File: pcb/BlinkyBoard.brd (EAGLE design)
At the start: 25.2 x 10 mm, 27 parts, among them Q1 16 MHz

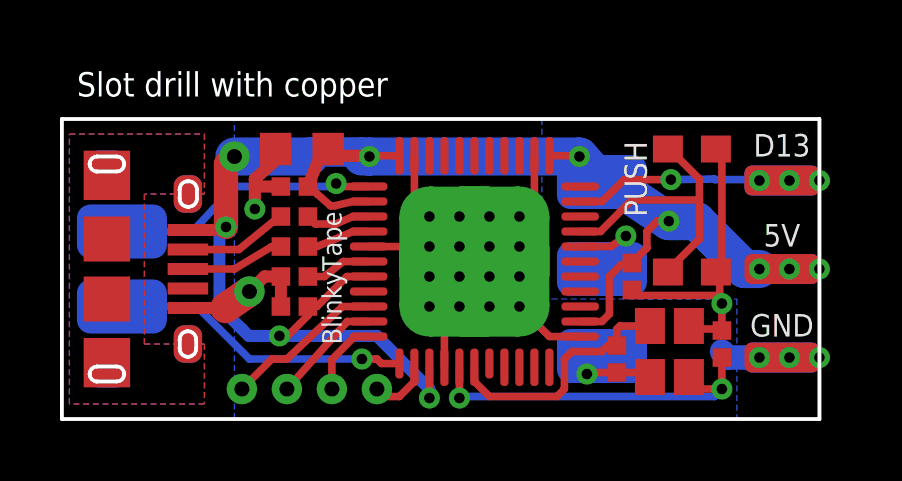
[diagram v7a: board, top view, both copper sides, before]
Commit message: PCB: Make LED connector holes bigger as per Bunnie's suggestion. Move the BlinkyTape logo a bit.
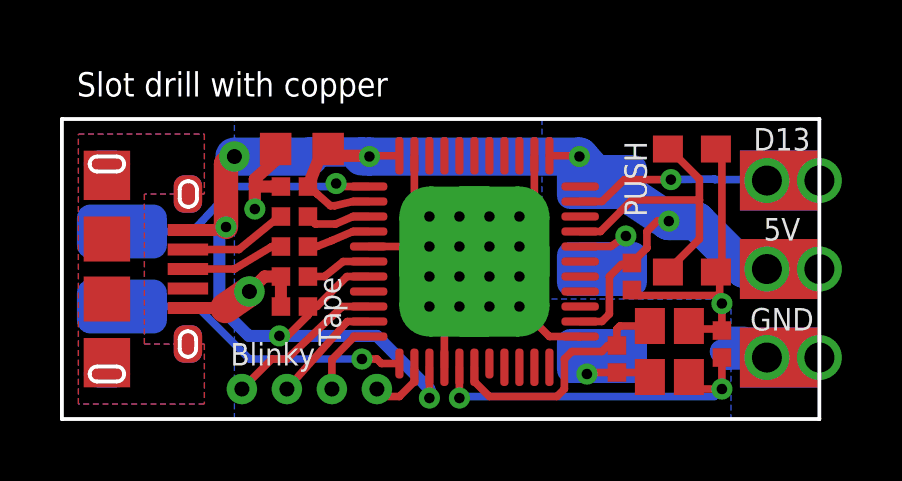
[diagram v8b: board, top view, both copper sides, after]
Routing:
- net VCC: track 55.1 -> 54.6 mm, vias 9 -> 8
- net D13: track 8.66 -> 8.99 mm, vias 4 -> 3
- net GND: track 36.1 -> 36.4 mm, vias 6 -> 5
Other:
- board text added: "7/13"
- board text added: "Blinky"
- board text added: "Rev E"
- board text added: "Tape"
- board text removed: "5/13"
- board text removed: "BlinkyTape"
- board text removed: "Rev Exx"
